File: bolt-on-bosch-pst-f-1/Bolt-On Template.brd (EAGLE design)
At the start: 42 x 72 mm, 10 parts

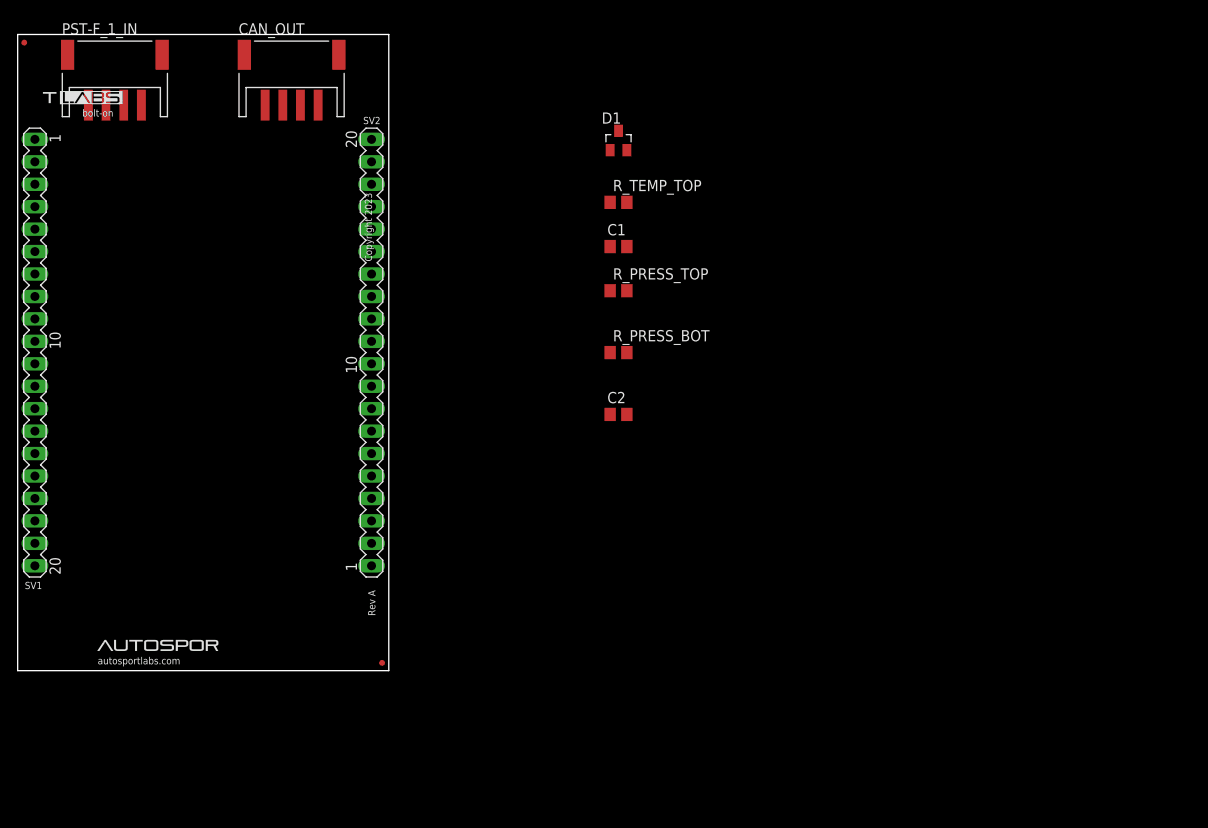
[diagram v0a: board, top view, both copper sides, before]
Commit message: designed circuit board for bosch sensor
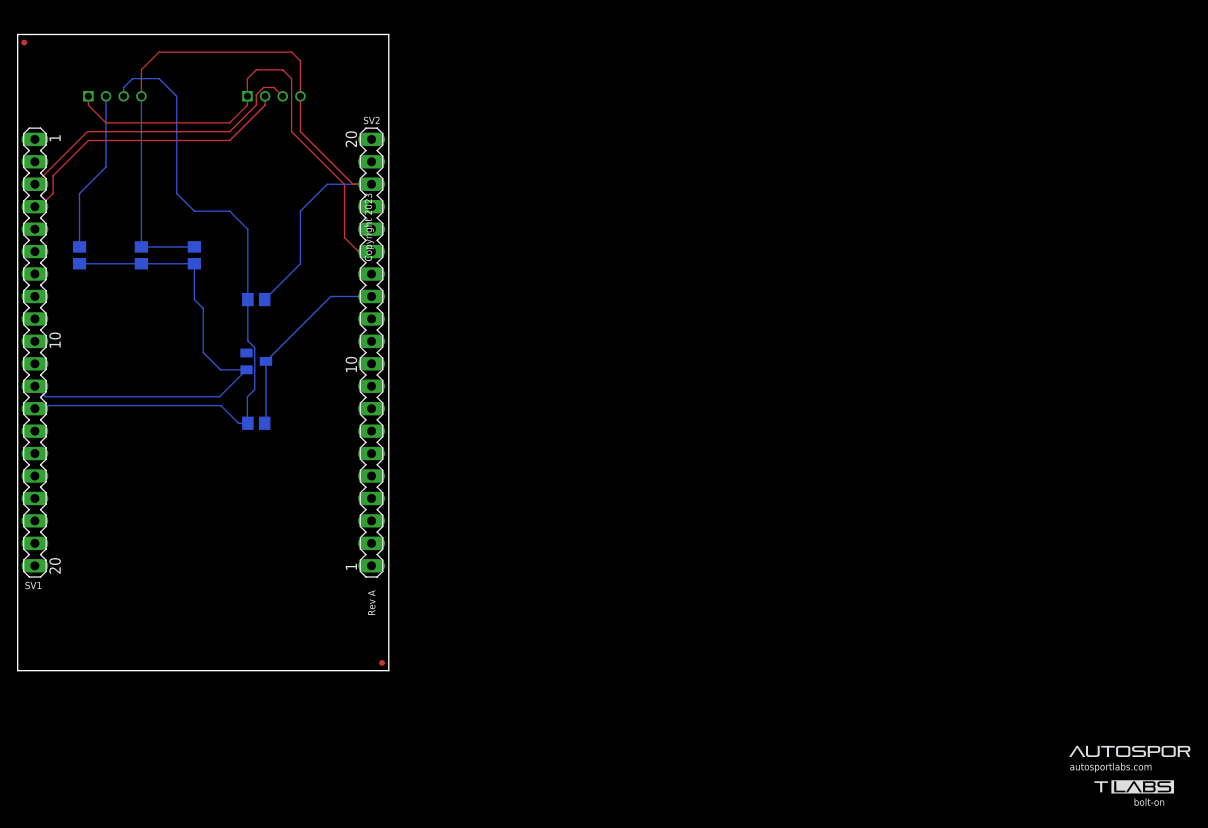
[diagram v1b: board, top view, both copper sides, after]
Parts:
- removed CAN_OUT: (no value), JST PH Library:S4B-PH-SM4-TB
- added CAN_X2_5V: (no value), JST PH Library:S4B-PH-K-S
- PST-F_1_IN: device JST PH Library:S4B-PH-SM4-TB -> JST PH Library:S4B-PH-K-S
- moved R_PRESS_TOP 61.1 mm to (7.00, 47.0), flipped to the bottom, turned to 90 degrees
- moved R_PRESS_BOT 55.1 mm to (14.0, 47.0), flipped to the bottom, turned to 90 degrees
- moved D1 48.0 mm to (27.0, 35.0), flipped to the bottom, turned to 90 degrees
- moved R_TEMP_TOP 48.0 mm to (27.0, 28.0), flipped to the bottom, turned to 180 degrees
- moved C1 48.0 mm to (20.0, 47.0), flipped to the bottom, turned to 270 degrees
- moved C2 43.0 mm to (27.0, 42.0), flipped to the bottom
- flipped PST-F_1_IN to the bottom
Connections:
- removed net +12V: PST-F_1_IN.1, SV2.19, SV2.20
- new net N$2: SV2.19, SV2.20
- net +5V: now also CAN_X2_5V.1, PST-F_1_IN.1; no longer CAN_OUT.1
- net CAN2H: now also CAN_X2_5V.3; no longer CAN_OUT.3
- net CAN2L: now also CAN_X2_5V.2; no longer CAN_OUT.2
- net GND: now also CAN_X2_5V.4; no longer CAN_OUT.4
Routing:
- net GND: track 0.00 -> 85.1 mm
- net TEMP_ADC: track 0.00 -> 76.8 mm
- net PRESS_ADC: track 0.00 -> 54.9 mm
- net +5V: track 0.00 -> 53.7 mm
- net CAN2H: track 0.00 -> 33.7 mm
- net CAN2L: track 0.00 -> 33.0 mm
- net V+: track 0.00 -> 22.1 mm
- net N$1: track 0.00 -> 18.3 mm
- net IO2: track 0.71 -> 0.00 mm

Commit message: added labels to circuit board
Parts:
- moved C1 9.00 mm to (20.0, 38.0)
- moved R_PRESS_BOT 9.00 mm to (14.0, 38.0)
- moved R_PRESS_TOP 9.00 mm to (7.00, 38.0)
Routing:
- net PRESS_ADC: track 54.9 -> 45.9 mm
- net N$1: track 18.3 -> 27.3 mm
- net GND: track 85.1 -> 94.1 mm
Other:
- board text added: "5V"
- board text added: "CAN_H"
- board text added: "CAN_L"
- board text added: "GND"
- board text added: "PRESS_SIG"
- board text added: "TEMP_SIG"
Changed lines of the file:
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@@
 <wire x1="42" y1="0" x2="0" y2="0" width="0" layer="20"/>
 <dimension x1="0" y1="72" x2="42" y2="72" x3="21" y3="79" textsize="1.778" layer="47"/>
+<text x="32" y="62" size="1.016" layer="21" rot="R90" align="center-right">GND</text>
+<text x="26" y="62" size="1.016" layer="21" rot="R90" align="center-right">5V</text>
+<text x="28" y="62" size="1.016" layer="21" rot="R90" align="center-right">CAN_L</text>
+<text x="30" y="62" size="1.016" layer="21" rot="R90" align="center-right">CAN_H</text>
+<text x="14" y="62" size="1.016" layer="21" rot="R90" align="center-right">GND</text>
+<text x="8" y="62" size="1.016" layer="21" rot="R90" align="center-right">5V</text>
+<text x="12" y="62" size="1.016" layer="21" rot="R90" align="center-right">TEMP_SIG</text>
+<text x="10" y="62" size="1.016" layer="21" rot="R90" align="center-right">PRESS_SIG </text>
 </plain>
 <attributes>
@@
 <attribute name="VALUE" x="26.365" y="30.54" size="1.27" layer="28" rot="MR180"/>
 </element>
-<element name="C1" library="rcl" library_urn="urn:adsk.eagle:library:334" package="C0805" package3d_urn="urn:adsk.eagle:package:23617/2" value="0.1µF" x="20" y="47" smashed="yes" rot="MR270">
-<attribute name="NAME" x="18.73" y="48.27" size="1.27" layer="26" rot="MR270"/>
-<attribute name="POPULARITY" value="88" x="20" y="47" size="1.778" layer="28" rot="MR270" display="off"/>
-<attribute name="SPICEPREFIX" value="C" x="20" y="47" size="1.778" layer="28" rot="MR270" display="off"/>
-<attribute name="VALUE" x="22.54" y="48.27" size="1.27" layer="28" rot="MR270"/>
-</element>
-<element name="R_PRESS_TOP" library="rcl" library_urn="urn:adsk.eagle:library:334" package="R0805" package3d_urn="urn:adsk.eagle:package:23553/2" value="4.7kΩ" x="7" y="47" smashed="yes" rot="MR90">
-<attribute name="NAME" x="8.27" y="41.365" size="1.27" layer="26" rot="MR90"/>
-<attribute name="POPULARITY" value="86" x="7" y="47" size="1.778" layer="28" rot="MR90" display="off"/>
-<attribute name="SPICEPREFIX" value="R" x="7" y="47" size="1.778" layer="28" rot="MR90" display="off"/>
-<attribute name="VALUE" x="4.46" y="44.365" size="1.27" layer="28" rot="MR90"/>
-</element>
-<element name="R_PRESS_BOT" library="rcl" library_urn="urn:adsk.eagle:library:334" package="R0805" package3d_urn="urn:adsk.eagle:package:23553/2" value="10kΩ" x="14" y="47" smashed="yes" rot="MR90">
-<attribute name="NAME" x="15.27" y="41.365" size="1.27" layer="26" rot="MR90"/>
-<attribute name="POPULARITY" value="86" x="14" y="47" size="1.778" layer="28" rot="MR90" display="off"/>
-<attribute name="SPICEPREFIX" value="R" x="14" y="47" size="1.778" layer="28" rot="MR90" display="off"/>
-<attribute name="VALUE" x="11.46" y="45.365" size="1.27" layer="28" rot="MR90"/>
+<element name="C1" library="rcl" library_urn="urn:adsk.eagle:library:334" package="C0805" package3d_urn="urn:adsk.eagle:package:23617/2" value="0.1µF" x="20" y="38" smashed="yes" rot="MR270">
+<attribute name="NAME" x="18.73" y="39.27" size="1.27" layer="26" rot="MR270"/>
+<attribute name="POPULARITY" value="88" x="20" y="38" size="1.778" layer="28" rot="MR270" display="off"/>
+<attribute name="SPICEPREFIX" value="C" x="20" y="38" size="1.778" layer="28" rot="MR270" display="off"/>
+<attribute name="VALUE" x="22.54" y="39.27" size="1.27" layer="28" rot="MR270"/>
+</element>
+<element name="R_PRESS_TOP" library="rcl" library_urn="urn:adsk.eagle:library:334" package="R0805" package3d_urn="urn:adsk.eagle:package:23553/2" value="4.7kΩ" x="7" y="38" smashed="yes" rot="MR90">
+<attribute name="NAME" x="8.27" y="32.365" size="1.27" layer="26" rot="MR90"/>
+<attribute name="POPULARITY" value="86" x="7" y="38" size="1.778" layer="28" rot="MR90" display="off"/>
+<attribute name="SPICEPREFIX" value="R" x="7" y="38" size="1.778" layer="28" rot="MR90" display="off"/>
+<attribute name="VALUE" x="4.46" y="35.365" size="1.27" layer="28" rot="MR90"/>
+</element>
+<element name="R_PRESS_BOT" library="rcl" library_urn="urn:adsk.eagle:library:334" package="R0805" package3d_urn="urn:adsk.eagle:package:23553/2" value="10kΩ" x="14" y="38" smashed="yes" rot="MR90">
+<attribute name="NAME" x="15.27" y="32.365" size="1.27" layer="26" rot="MR90"/>
+<attribute name="POPULARITY" value="86" x="14" y="38" size="1.778" layer="28" rot="MR90" display="off"/>
+<attribute name="SPICEPREFIX" value="R" x="14" y="38" size="1.778" layer="28" rot="MR90" display="off"/>
+<attribute name="VALUE" x="11.46" y="36.365" size="1.27" layer="28" rot="MR90"/>
 </element>
 <element name="C2" library="rcl" library_urn="urn:adsk.eagle:library:334" package="C0805" package3d_urn="urn:adsk.eagle:package:23617/2" value="0.1µF" x="27" y="42" smashed="yes" rot="MR0">
@@
 <contactref element="C1" pad="1"/>
 <contactref element="C2" pad="1"/>
-<wire x1="20.125828125" y1="47.824171875" x2="20" y2="47.95" width="0.1524" layer="16"/>
+<wire x1="20.125828125" y1="38.824171875" x2="20" y2="38.95" width="0.1524" layer="16"/>
 <contactref element="CAN_X2_5V" pad="4"/>
 <contactref element="PST-F_1_IN" pad="4"/>
@@
 <wire x1="27.9543" y1="41.95" x2="27.95" y2="42" width="0.1524" layer="16"/>
 <wire x1="28" y1="42.0059375" x2="27.95" y2="42" width="0.1524" layer="16"/>
-<wire x1="14" y1="47.95" x2="20" y2="47.95" width="0.1524" layer="16"/>
-<wire x1="14" y1="47.95" x2="14" y2="65" width="0.1524" layer="16"/>
+<wire x1="14" y1="38.95" x2="20" y2="38.95" width="0.1524" layer="16"/>
+<wire x1="14" y1="38.95" x2="14" y2="65" width="0.1524" layer="16"/>
 <wire x1="27.95" y1="42" x2="32" y2="46.05" width="0.1524" layer="16"/>
 <wire x1="32" y1="46.05" x2="32" y2="52" width="0.1524" layer="16"/>
@@
 <wire x1="40.05" y1="49.97" x2="40.05" y2="52.51" width="0" layer="19" extent="1-1"/>
 <wire x1="40.05" y1="55.05" x2="40.05" y2="52.51" width="0" layer="19" extent="1-1"/>
+<wire x1="14" y1="65" x2="14" y2="38.95" width="0" layer="19"/>
 </signal>
 <signal name="CAN1L">
@@
 <wire x1="10" y1="65" x2="10" y2="57" width="0.1524" layer="16"/>
 <wire x1="10" y1="57" x2="7" y2="54" width="0.1524" layer="16"/>
-<wire x1="7" y1="54" x2="7" y2="47.95" width="0.1524" layer="16"/>
+<wire x1="7" y1="54" x2="7" y2="38.95" width="0.1524" layer="16"/>
 </signal>
 <signal name="PRESS_ADC">
@@
 <contactref element="R_PRESS_BOT" pad="1"/>
 <contactref element="C1" pad="2"/>
-<wire x1="7" y1="46.05" x2="14" y2="46.05" width="0.1524" layer="16"/>
-<wire x1="14" y1="46.05" x2="20" y2="46.05" width="0.1524" layer="16"/>
-<wire x1="20" y1="46.05" x2="20.05" y2="46" width="0.1524" layer="16"/>
-<wire x1="20" y1="42" x2="21" y2="41" width="0.1524" layer="16"/>
-<wire x1="21" y1="41" x2="21" y2="36" width="0.1524" layer="16"/>
-<wire x1="21" y1="36" x2="22.95" y2="34.05" width="0.1524" layer="16"/>
-<wire x1="20" y1="46.05" x2="20" y2="42" width="0.1524" layer="16"/>
+<wire x1="7" y1="37.05" x2="14" y2="37.05" width="0.1524" layer="16"/>
+<wire x1="14" y1="37.05" x2="20" y2="37.05" width="0.1524" layer="16"/>
+<wire x1="20" y1="37.05" x2="20.05" y2="37" width="0.1524" layer="16"/>
+<wire x1="20" y1="37" x2="22.95" y2="34.05" width="0.1524" layer="16"/>
+<wire x1="20" y1="37.05" x2="20" y2="37" width="0.1524" layer="16"/>
 <wire x1="25.9" y1="34.05" x2="22.85" y2="31" width="0.1524" layer="16"/>
 <wire x1="22.95" y1="34.05" x2="25.9" y2="34.05" width="0.1524" layer="16"/>

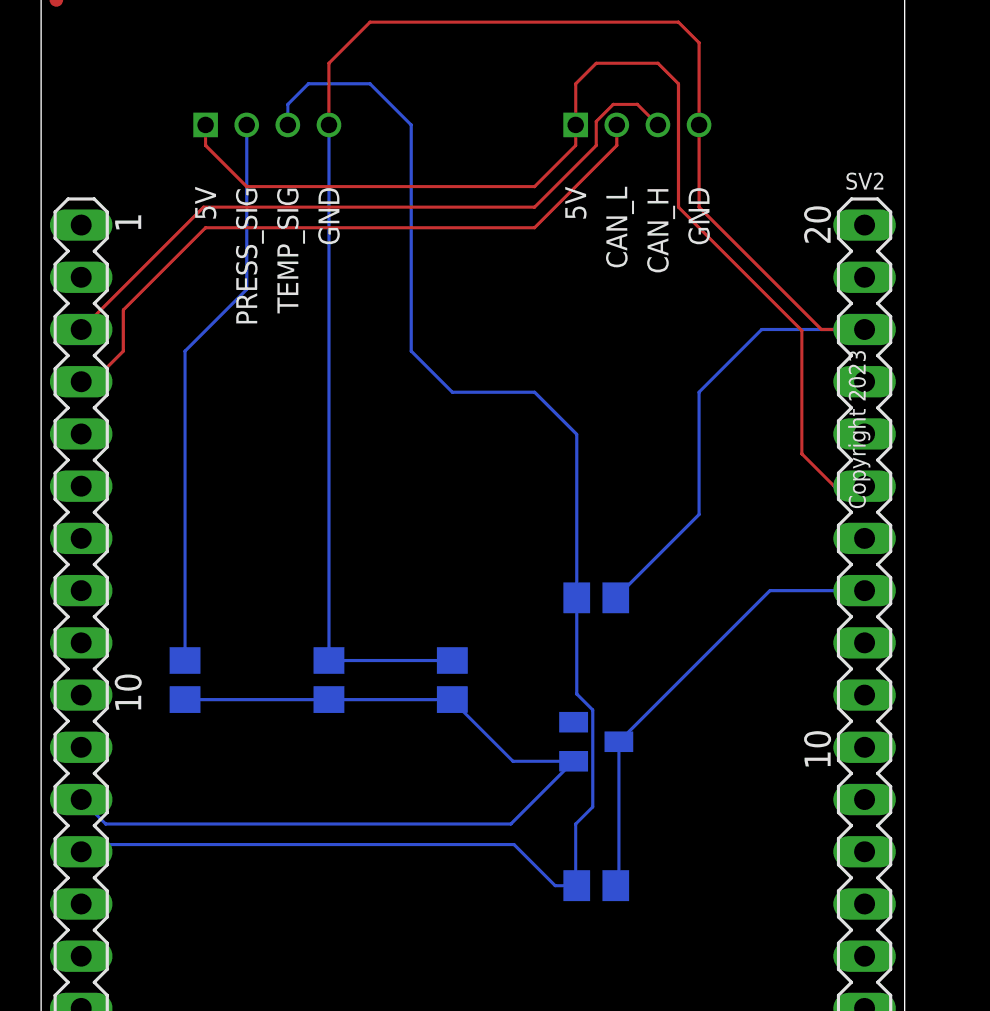
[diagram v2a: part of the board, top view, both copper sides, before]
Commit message: added readme for daughter board design
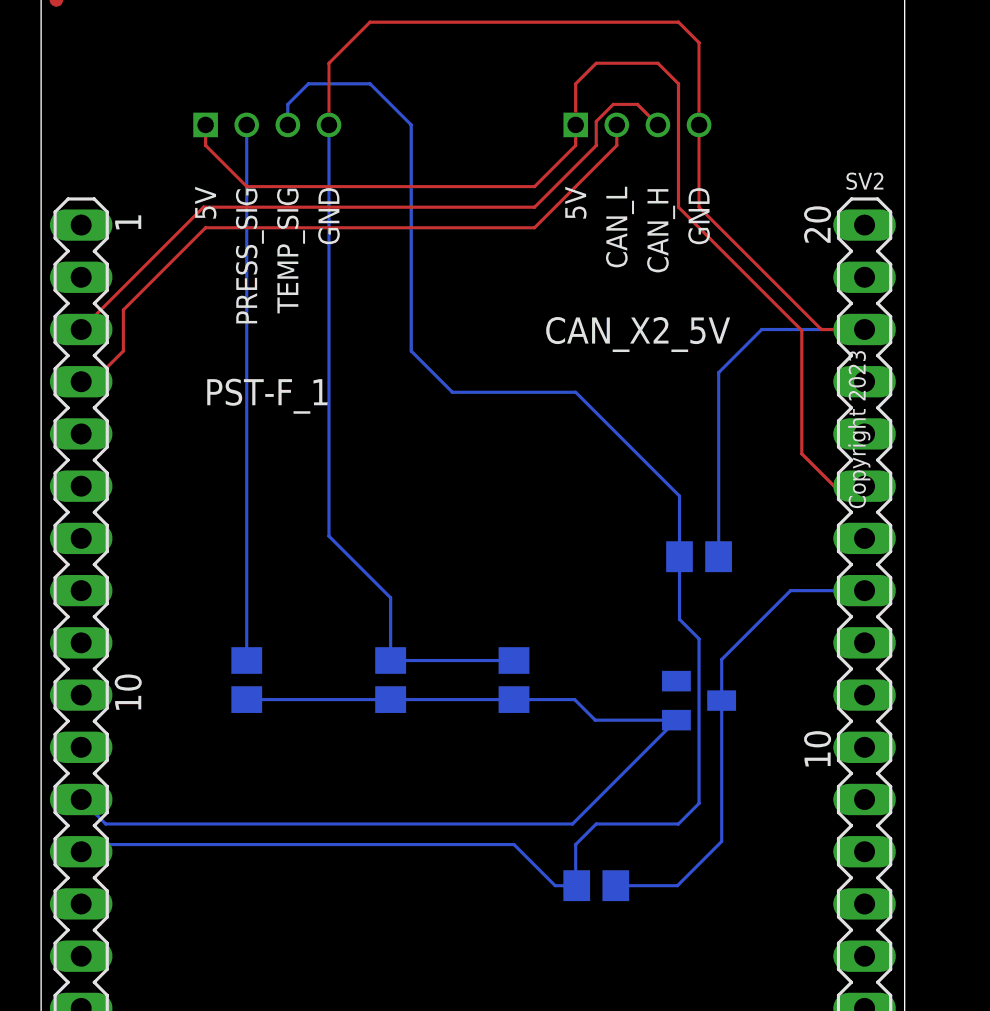
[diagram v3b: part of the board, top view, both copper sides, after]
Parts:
- R_PRESS_TOP: value 4.7kΩ -> 5.6kΩ
- R_TEMP_TOP: value 100kΩ -> 30kΩ
- moved C2 5.39 mm to (32.0, 44.0)
- moved D1 5.39 mm to (32.0, 37.0)
- moved C1 3.00 mm to (23.0, 38.0)
- moved R_PRESS_BOT 3.00 mm to (17.0, 38.0)
- moved R_PRESS_TOP 3.00 mm to (10.0, 38.0)
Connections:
- net N$2 renamed 12V
- net V+ renamed +3.3V
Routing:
- net TEMP_ADC: track 76.8 -> 84.5 mm
- net PRESS_ADC: track 45.9 -> 52.9 mm
- net GND: track 94.1 -> 91.4 mm
- net N$1: track 27.3 -> 26.0 mm
- net +3.3V: track 22.1 -> 23.2 mm
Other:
- board text added: "CAN_X2_5V"
- board text added: "PST-F_1"
